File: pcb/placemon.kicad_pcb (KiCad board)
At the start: 2 copper layers, 65 x 30 mm, 35 parts, among them J1 RPi_GPIO, Q1 BSS138, Q2 BSS138, U1 CAT24C128, U2 LSM303AGR, U3 LP5907MFX-2.8, U4 VL6180V1NR/1, U5 SHT30-DIS, U6 GMA4030H11-F26

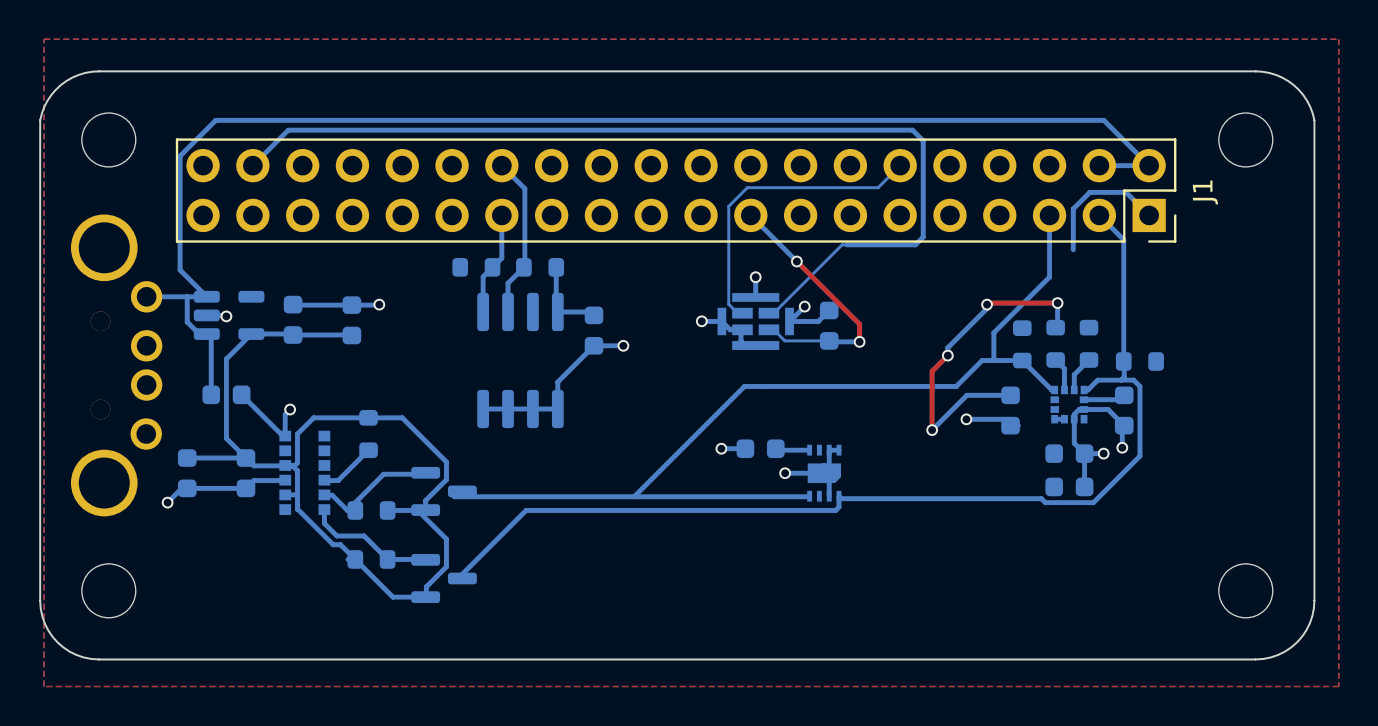
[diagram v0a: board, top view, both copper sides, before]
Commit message: Try to fix position of pin header
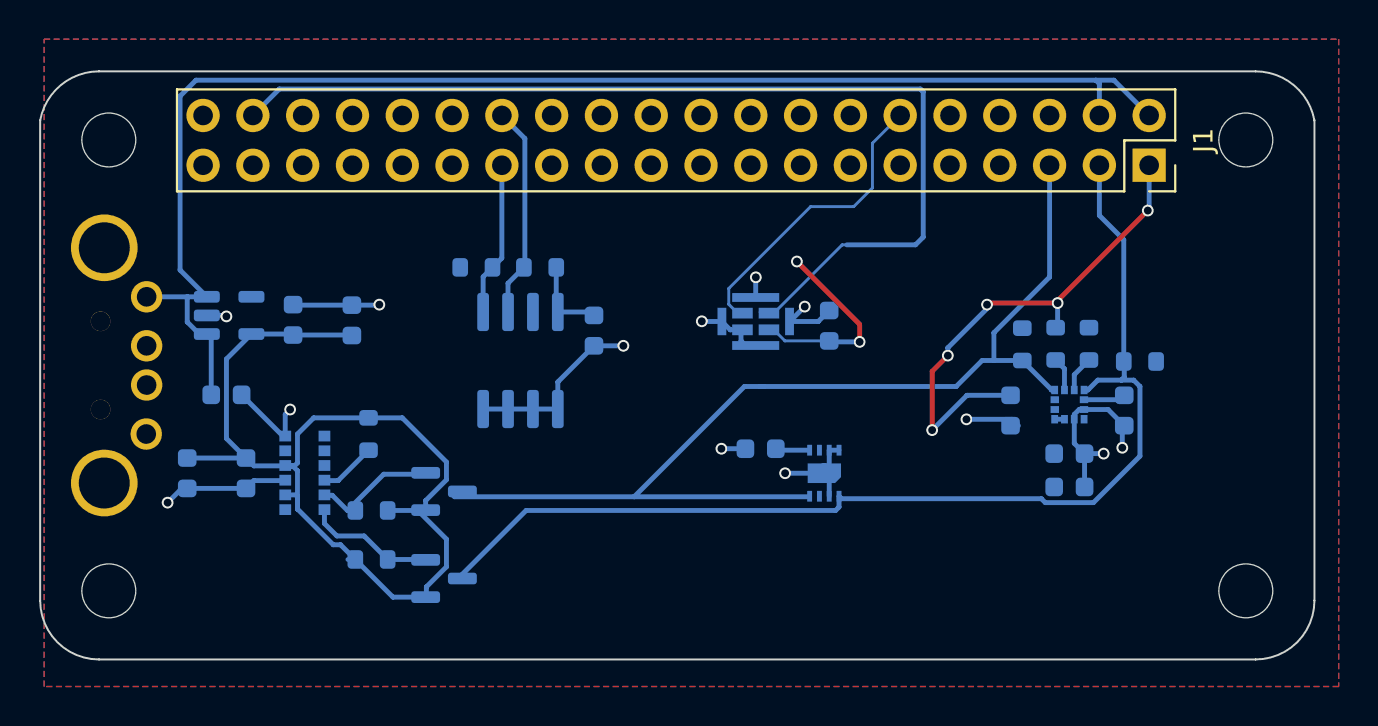
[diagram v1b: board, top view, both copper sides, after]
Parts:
- moved J1 2.56 mm to (69.1, 29.3)
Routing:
- net SDA: track 53.6 -> 56.2 mm
- net SCK: track 52.3 -> 54.9 mm
- net ID_SD: track 5.32 -> 7.88 mm
- net ID_SC: track 8.31 -> 10.9 mm
- net data: track 49.6 -> 51.7 mm
- net +3V3: track 45.4 -> 43.6 mm, vias 6 -> 7
- net +5V: track 70.2 -> 72.0 mm
